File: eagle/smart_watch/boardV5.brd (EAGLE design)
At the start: 63.6 x 36.1 mm, 67 parts, among them IC1 SC16IS750, U1 MCP73831, U2 TPS61200, U3 MAX1704X, U4 V_REG_LDOSMD, Y1 16MHz, Y2 12.28MHz

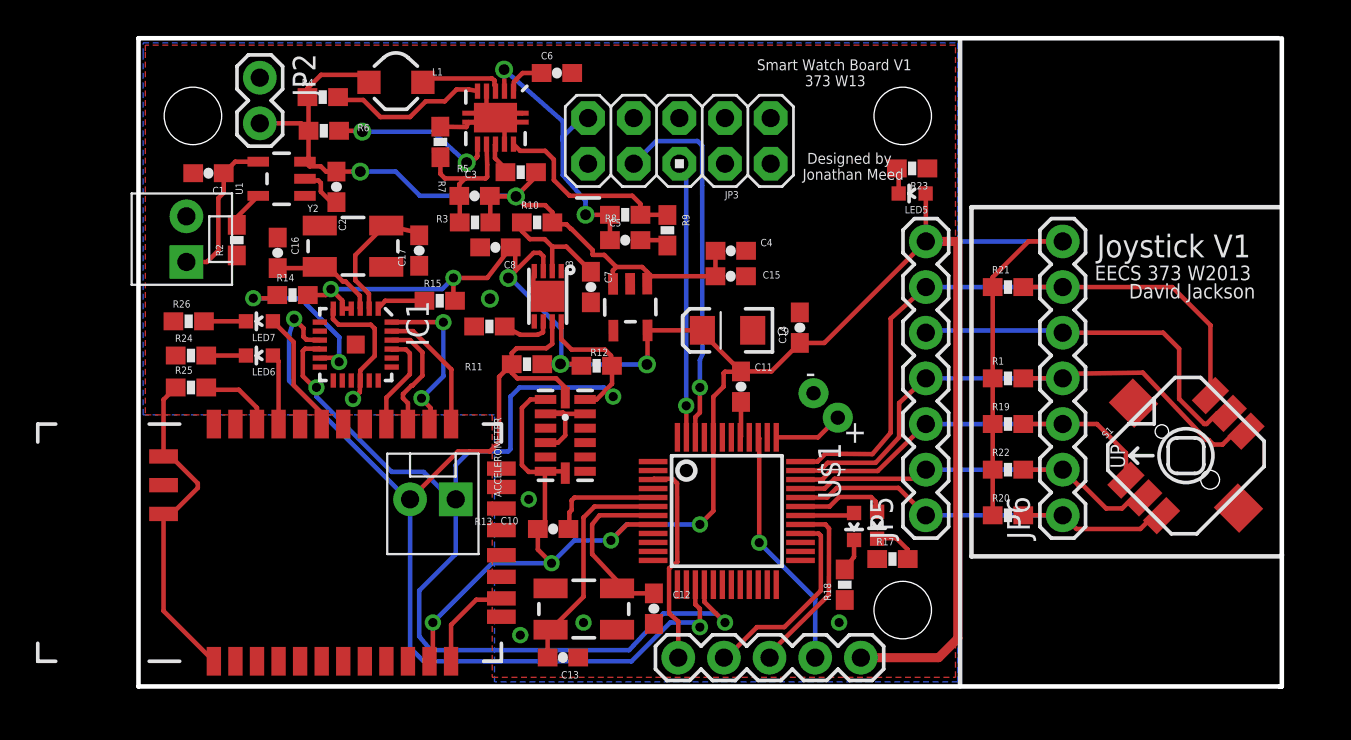
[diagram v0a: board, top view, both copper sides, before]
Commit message: Made a few minor changes to board V4, added V5 with edits for printing. TODO: Wiring of board V5. See email for other additions
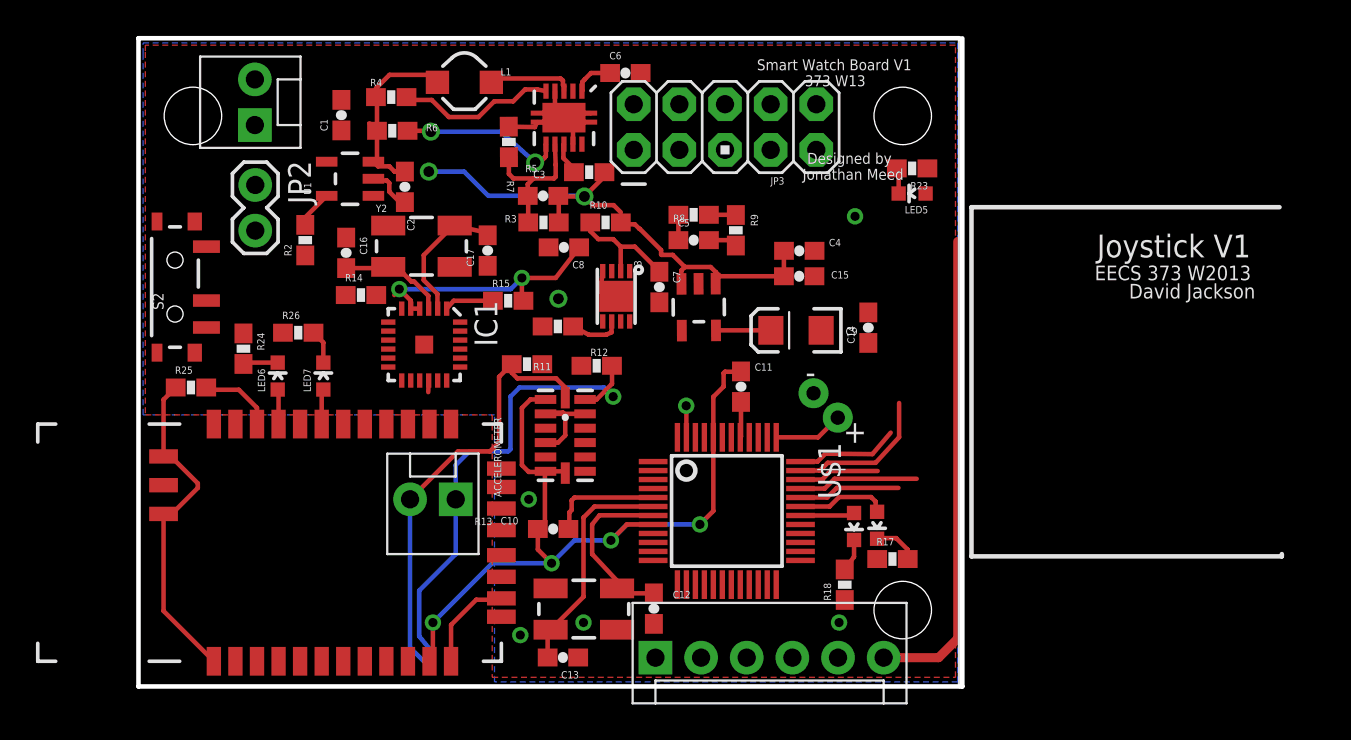
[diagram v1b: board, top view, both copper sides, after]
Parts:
- removed JP5, JP6: (no value), SparkFun-Connectors:1X07
- removed R1, R19, R20, R21, R22: 10k, SparkFun-Resistors:0603-RES
- removed S1: (no value), SparkFun-Electromechanical:JOYSTICK_MINI
- added S2: (no value), SparkFun-Electromechanical:SWITCH-SPST-SMD-A
- JP4: device SparkFun-Connectors:1X05 -> SparkFun-Connectors:MOLEX-1X6
- moved RECHARGE 8.52 mm to (6.48, 31.2)
- moved C1 8.07 mm to (11.3, 31.8), turned to 90 degrees
- moved R26 6.13 mm to (8.89, 19.7)
- moved JP2 5.97 mm to (6.50, 27.9)
- moved LED7 4.68 mm to (10.3, 17.3), turned to 0 degrees
- moved C14 3.81 mm to (40.6, 20.0)
- moved C15 3.81 mm to (36.8, 22.8)
- moved C4 3.81 mm to (36.8, 24.2)
- moved C5 3.81 mm to (30.9, 24.8)
- moved C7 3.81 mm to (29.0, 22.2)
- moved L1 3.81 mm to (18.1, 33.6)
- moved R15 3.81 mm to (20.6, 21.5)
- moved R7 3.81 mm to (20.6, 30.3)
- moved R8 3.81 mm to (30.9, 26.2)
- moved U2 3.81 mm to (23.7, 31.7)
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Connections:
- new net N$14: C2.1, S2.1, U1.3
- new net N$26: JP2.2, S2.2
- net 3.3V: now also JP4.6; no longer JP4.5, JP5.7, JP6.7, R1.1, R19.1, R20.1, R21.1, R22.1
- net 3.3V_OUT: now also JP3.9; no longer JP3.10
- net GND: now also JP3.10, JP3.7, JP4.1; no longer JP3.8, JP3.9, JP5.5, JP6.5, S1.GND
- net JCENTER: no longer JP5.2, JP6.2, R22.2, S1.CTR
- net JDOWN: no longer JP5.4, JP6.4, R1.2, S1.D
- net JLEFT: no longer JP5.1, JP6.1, R20.2, S1.C
- net JRIGHT: no longer JP5.6, JP6.6, R21.2, S1.B
- net JTAG_RESETX: now also JP4.2; no longer JP4.1
- net JTAG_TCLK_SWCLKX: now also JP4.4; no longer JP4.3
- net JTAG_TDO_SWOX: now also JP4.3; no longer JP4.2
- net JTAG_TMS_SWDIOX: now also JP4.5; no longer JP4.4
- net JUP: no longer JP5.3, JP6.3, R19.2, S1.A
- net SCIO1: now also JP3.5; no longer JP3.6
- net SCIO2: now also JP3.3; no longer JP3.4
- net SCRESET: now also JP3.8; no longer JP3.7
- net SCRX: now also JP3.4; no longer JP3.3
- net SCTX: now also JP3.6; no longer JP3.5
- net VBATT: now also S2.3; no longer C2.1, JP2.2, U1.3
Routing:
- net 3.3V: track 158.4 -> 89.9 mm, vias 9 -> 6
- net SDA: track 66.2 -> 27.4 mm, vias 3 -> 1
- net SCL: track 62.9 -> 24.6 mm, vias 2 -> 0
- net JRIGHT: track 37.6 -> 5.75 mm
- net GND: track 81.6 -> 53.6 mm
- net JDOWN: track 32.4 -> 8.20 mm
- net SCRX: track 20.8 -> 0.00 mm, vias 1 -> 0
- net JUP: track 23.8 -> 4.50 mm
- net JLEFT: track 23.8 -> 5.67 mm
- net JCENTER: track 22.9 -> 6.69 mm
- net 5V: track 15.9 -> 1.41 mm, vias 2 -> 0
- net SCTX: track 15.4 -> 1.76 mm
- net JTAG_TMS_SWDIOX: track 13.6 -> 0.00 mm, vias 1 -> 0
- net JTAG_RESETX: track 11.6 -> 0.00 mm
- net JTAG_TDO_SWOX: track 11.2 -> 0.00 mm
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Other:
- board size 63.6 x 36.1 mm -> 45.8 x 36.1 mm

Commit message: Git commit. Finished and printed board V5
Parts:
- added JP5: (no value), SparkFun-Connectors:1X07
- added R1: 12k, SparkFun-Passives:0603-RES
- added R16: 1k, SparkFun-Passives:0603-RES
- Y2: value 12.28MHz -> 14.7456MHz
- moved S2 14.1 mm to (9.40, 34.3), turned to 0 degrees
- moved RECHARGE 11.2 mm to (2.79, 20.7)
- moved C1 10.8 mm to (7.03, 21.9), turned to 0 degrees
- moved JP2 4.88 mm to (1.81, 26.6), turned to 0 degrees
- moved C2 2.35 mm to (16.7, 29.2), turned to 0 degrees
- moved IC1 1.37 mm to (14.6, 18.5)
- moved R4 1.20 mm to (15.1, 32.2)
- moved LED7 0.76 mm to (9.53, 17.3)
- moved R15 0.28 mm to (20.4, 21.2)
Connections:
- removed net N$1: IC1.11, R14.1
- new net BATINT: R16.2, U$1.20, U3.5
- new net IRQB: IC1.11, R14.1, U$1.1
- net 3.3V: now also IC1.6, IC1.7, JP5.7, R1.2, R16.1
- net GND: now also JP3.8, JP5.5, Y1.2, Y1.4, Y2.2, Y2.4; no longer IC1.6, IC1.7, JP3.10
- net JCENTER: now also JP5.2
- net JDOWN: now also JP5.4
- net JLEFT: now also JP5.1
- net JRIGHT: now also JP5.6
- net JTAG_RESETX: now also R1.1
- net JUP: now also JP5.3
- net SCRESET: now also JP3.10; no longer JP3.8
- net VIBE_PWM: now also U$1.38
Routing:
- net 3.3V: track 89.9 -> 141.1 mm, vias 6 -> 8
- net IRQB: track 0.00 -> 40.6 mm, vias 0 -> 3
- net SCL: track 24.6 -> 60.9 mm, vias 0 -> 3
- net SDA: track 27.4 -> 62.8 mm, vias 1 -> 3
- net BATINT: track 0.00 -> 29.2 mm, vias 0 -> 4
- net SCTX: track 1.76 -> 25.0 mm
- net SCRX: track 0.00 -> 19.8 mm, vias 0 -> 1
- net JTAG_TMS_SWDIOX: track 0.00 -> 16.4 mm, vias 0 -> 1
- net 5V: track 1.41 -> 16.9 mm, vias 0 -> 2
- net RXB: track 0.00 -> 15.3 mm
- net JTAG_RESETX: track 0.00 -> 14.1 mm, vias 0 -> 1
- net VBUS: track 0.00 -> 13.6 mm
- net N$8: track 1.50 -> 13.5 mm
- net JTAG_TDO_SWOX: track 0.00 -> 11.7 mm, vias 0 -> 1
- net TXB: track 0.00 -> 11.5 mm, vias 0 -> 2
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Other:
- board text added: "Filippos Theodorakis"
- board text added: "Smart Watch Board V2"
- board text added: "Tony Lucches"
- board text removed: "Designed by"
- board text removed: "EECS 373 W2013"
- board text removed: "Joystick V1"
- board text removed: "Smart Watch Board V1"
